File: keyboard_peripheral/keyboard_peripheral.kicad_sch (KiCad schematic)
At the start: 46 parts, among them IC1 ATMEGA32U4-AU, J1 USB, J2 ISP, SW17 Reset, Y1 ABM3-16.000MHZ-D2Y-T

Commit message: Updates
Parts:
- C2, C3: value 22uf -> 22pf
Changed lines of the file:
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@@
 			)
 		)
-		(property "Value" "22uf"
+		(property "Value" "22pf"
 			(at 557.53 392.4299 0)
 			(effects
@@
 			)
 		)
-		(property "Value" "22uf"
+		(property "Value" "22pf"
 			(at 529.59 392.4299 0)
 			(effects

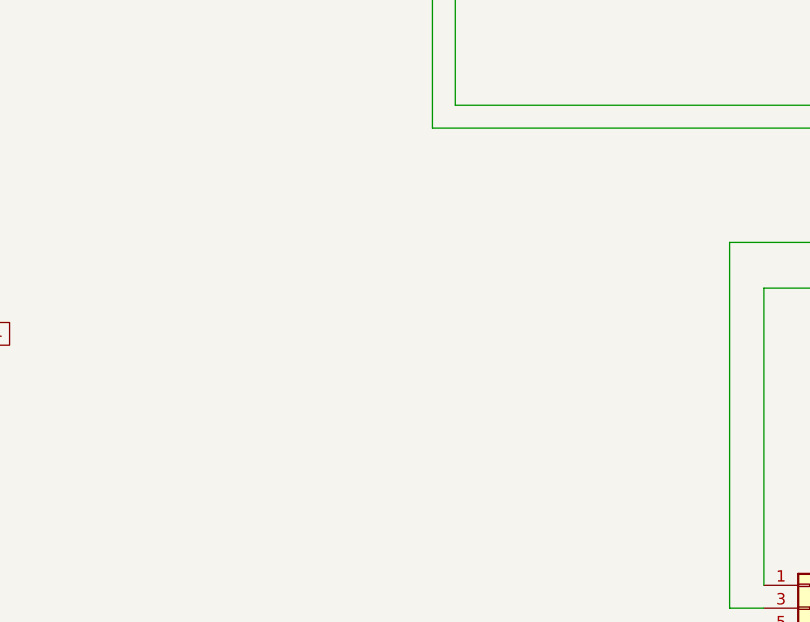
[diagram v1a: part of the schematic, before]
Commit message: Add LED; Unroute
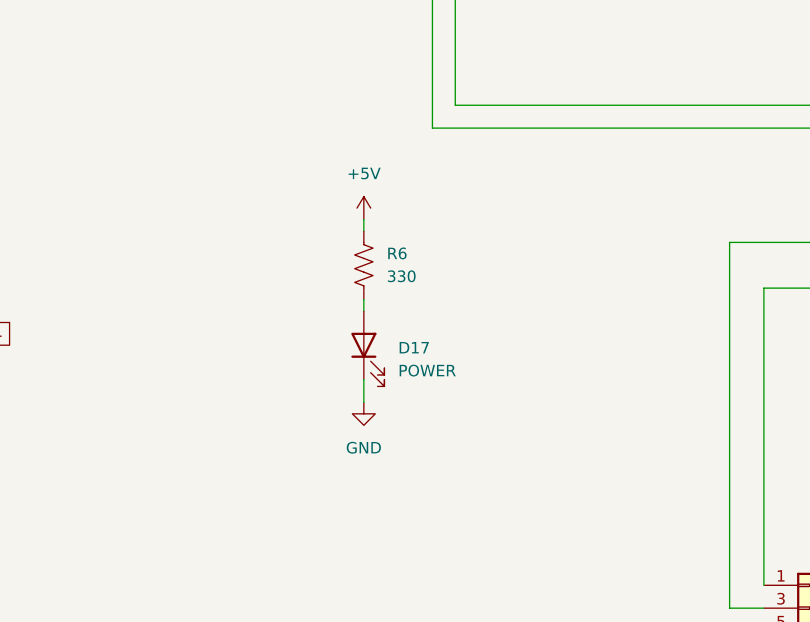
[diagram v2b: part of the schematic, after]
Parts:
- added D17: POWER, LED_SMD:LED_0201_0603Metric, symbol Device:LED
- added R6: 330, Resistor_SMD:R_0805_2012Metric, symbol Device:R_US
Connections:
- net +5V: now also R6.1
- net GND: now also D17.1 (K)
- new net: D17.2 (A), R6.2
